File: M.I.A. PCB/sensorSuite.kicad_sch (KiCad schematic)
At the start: 14 parts, among them U3 MMC5983MA, U4 ICM-45686, U5 MS5611-01BA, U6 TMP117xxDRV, U7 MAX-M10S, U8 KX134-1211

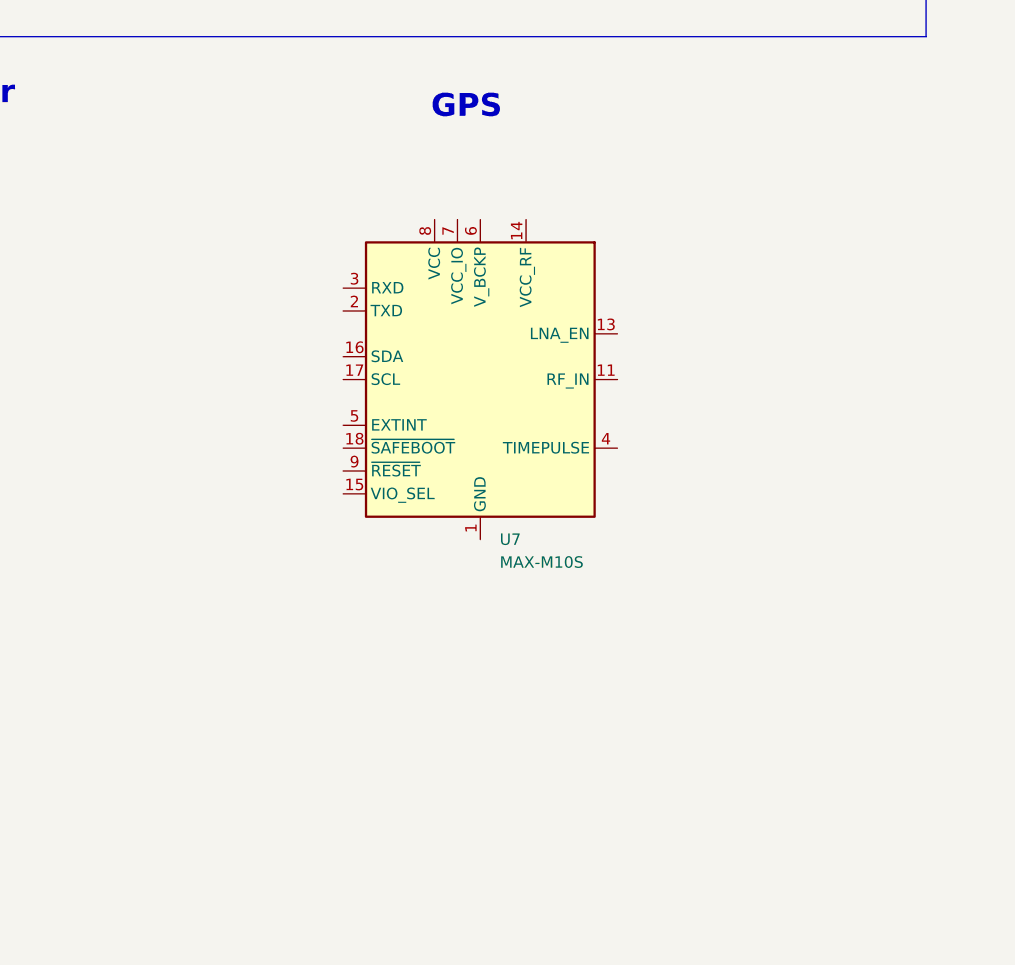
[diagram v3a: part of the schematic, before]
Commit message: Routed GPS Maybe Correctly
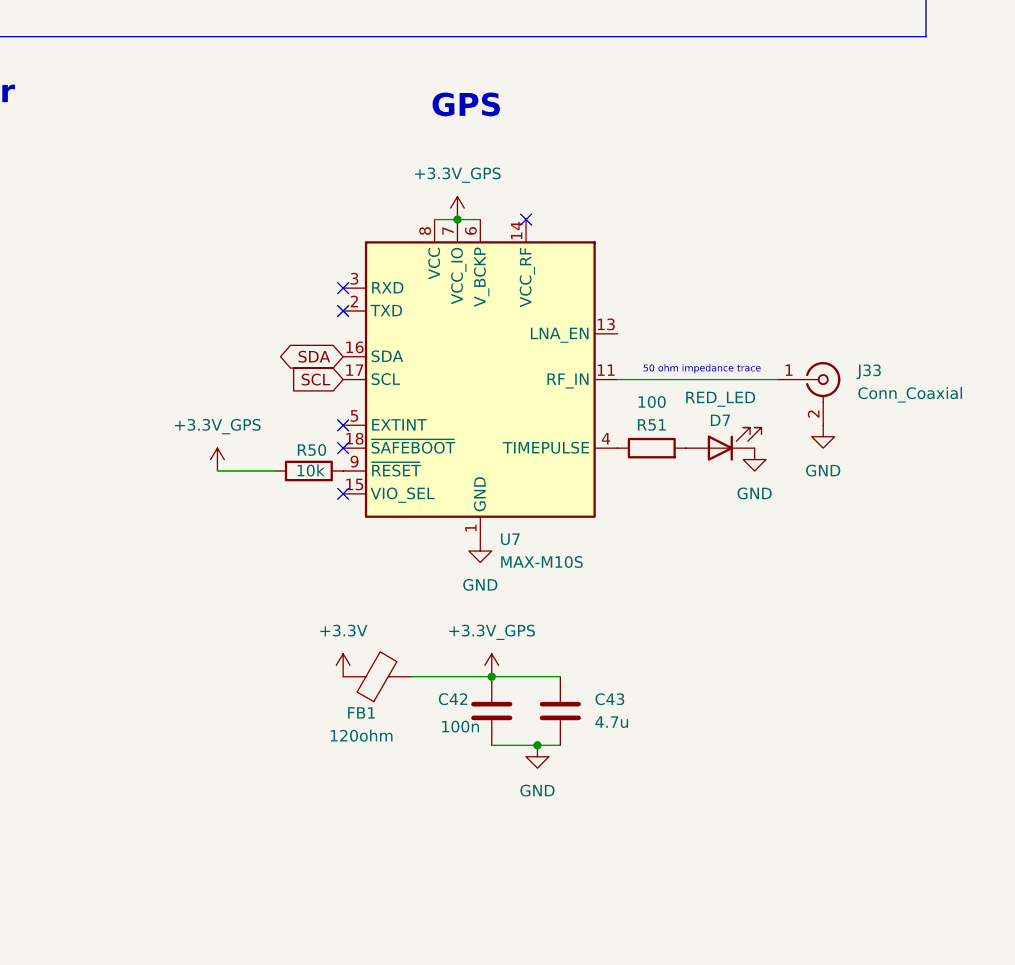
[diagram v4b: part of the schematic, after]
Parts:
- added C42: 100n, Capacitor_SMD:C_0603_1608Metric, symbol Device:C
- added C43: 4.7u, Capacitor_SMD:C_0805_2012Metric, symbol Device:C
- added D7: RED_LED, LED_SMD:LED_0805_2012Metric, symbol Device:LED
- added FB1: 120ohm, symbol Device:FerriteBead
- added J33: Conn_Coaxial, Connector_Coaxial:SMA_Amphenol_132134-11_Vertical, symbol Connector:Conn_Coaxial
- added R50: 10k, Resistor_SMD:R_0603_1608Metric, symbol Device:R
- added R51: 100, Resistor_SMD:R_0603_1608Metric, symbol Device:R
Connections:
- net +3.3V: now also FB1.1
- net GND: now also U7.1 (GND), U7.10 (GND), U7.12 (GND), C42.2, C43.2, D7.1 (K), J33.2 (Ext)
- net SCL: now also U7.17 (SCL)
- net SDA: now also U7.16 (SDA)
- net at U7.11 (RF_IN): now also J33.1 (In)
- net at U7.4 (TIMEPULSE): now also R51.1
- net +3.3V_GPS: now reaches U7.6 (V_BCKP)
- net +3.3V_GPS: now also U7.7 (VCC_IO), U7.8 (VCC), C42.1, C43.1, FB1.2, R50.1
- net at U7.9 (~{RESET}): now also R50.2
- new net: D7.2 (A), R51.2
- no-connect marks 8 -> 14
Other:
- note added: "50 ohm impedance trace"

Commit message: Added LEDs, Prepped for 4 layer conversion
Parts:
- FB1: footprint (none) -> Inductor_SMD:L_0805_2012Metric
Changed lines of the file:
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@@
 			)
 		)
-		(property "Footprint" ""
+		(property "Footprint" "Inductor_SMD:L_0805_2012Metric"
 			(at 208.28 145.288 90)
 			(effects

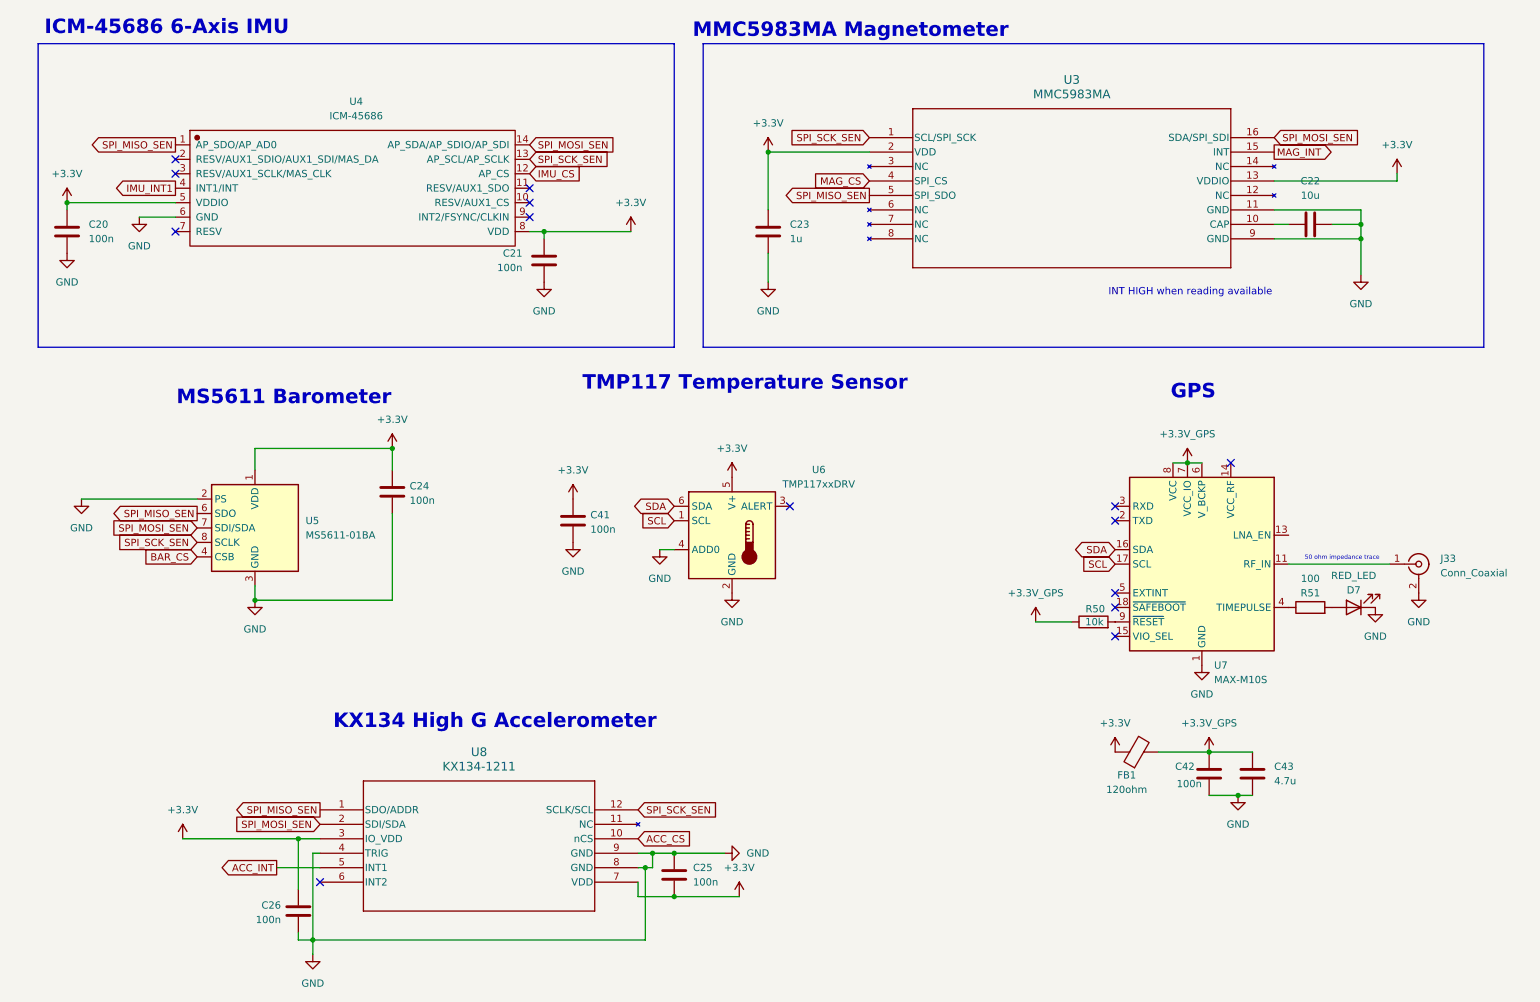
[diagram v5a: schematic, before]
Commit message: Updated top connectors to be TLM_SPI
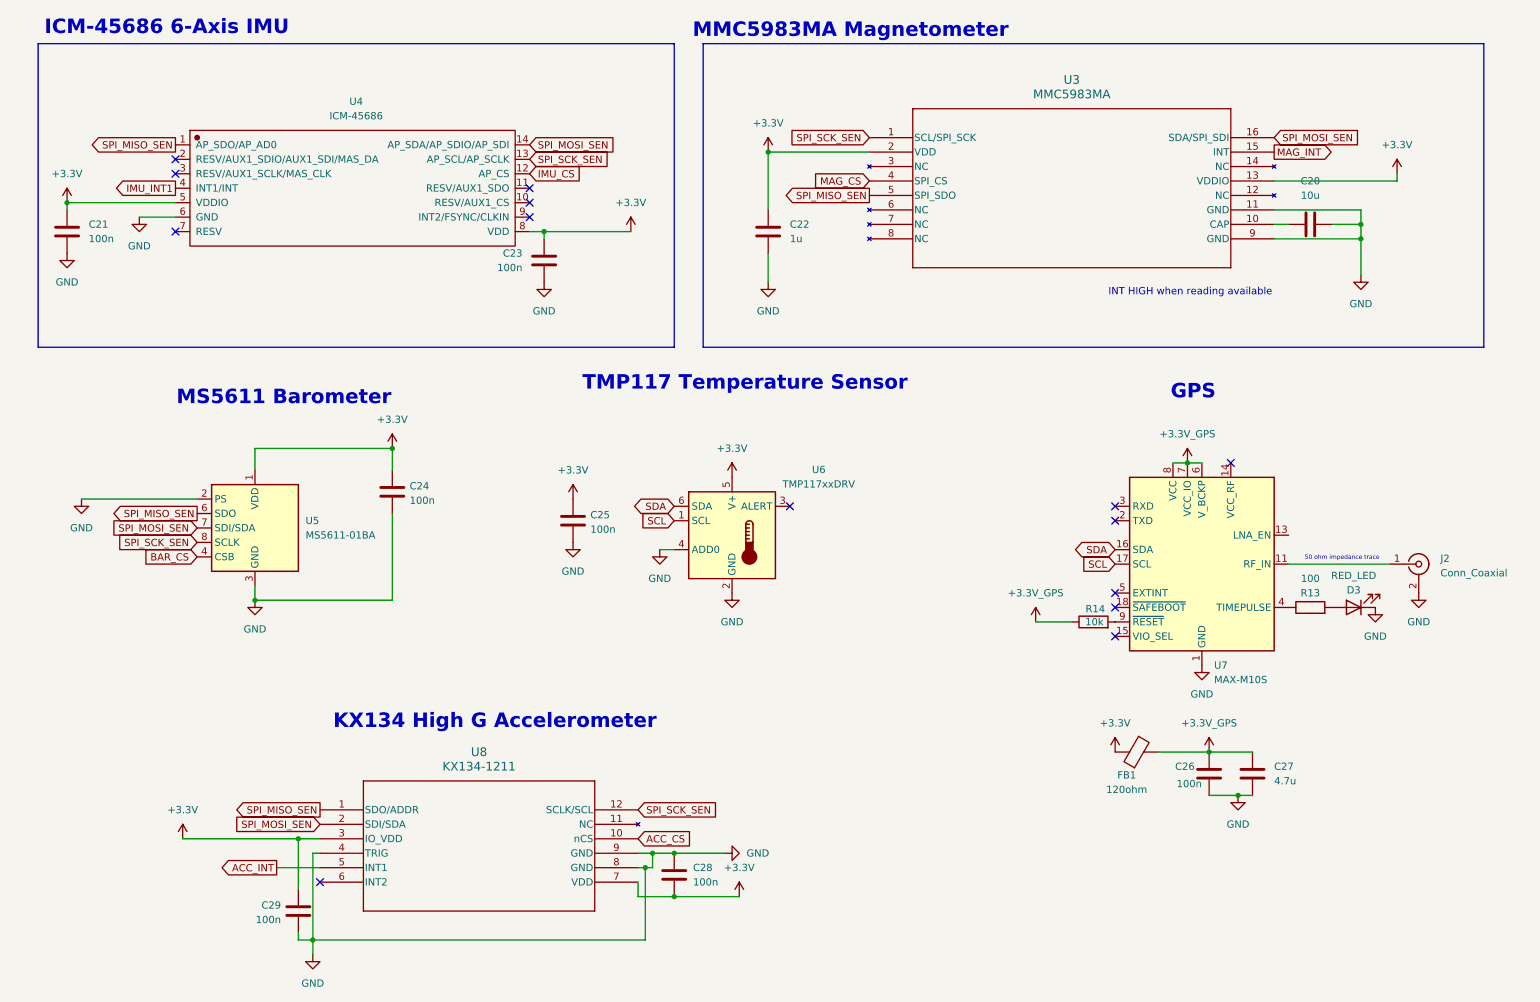
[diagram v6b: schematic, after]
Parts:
- renumbered C22 to C20, C20 to C21, C23 to C22, C21 to C23, C41 to C25, C42 to C26, C43 to C27, C25 to C28, C26 to C29, D7 to D3, J33 to J2, R51 to R13, R50 to R14

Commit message: More Small Updates/Improvements
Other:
- note added: "MAX-M10S GPS"
- note removed: "GPS"
- moved on the sheet: C24, C25, C26, C27, C28, C29, D3, FB1, J2, R13, R14, U5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
